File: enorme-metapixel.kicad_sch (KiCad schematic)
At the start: 22 parts, among them J1 VIN, J2 STRIP_0, J3 STRIP_1, J4 STRIP_2, J5 UART, J6 VIN, SW1 SW_RESET, SW2 SW_BOOT, U1 BD33FC0FP, U2 ESP32-WROOM-32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

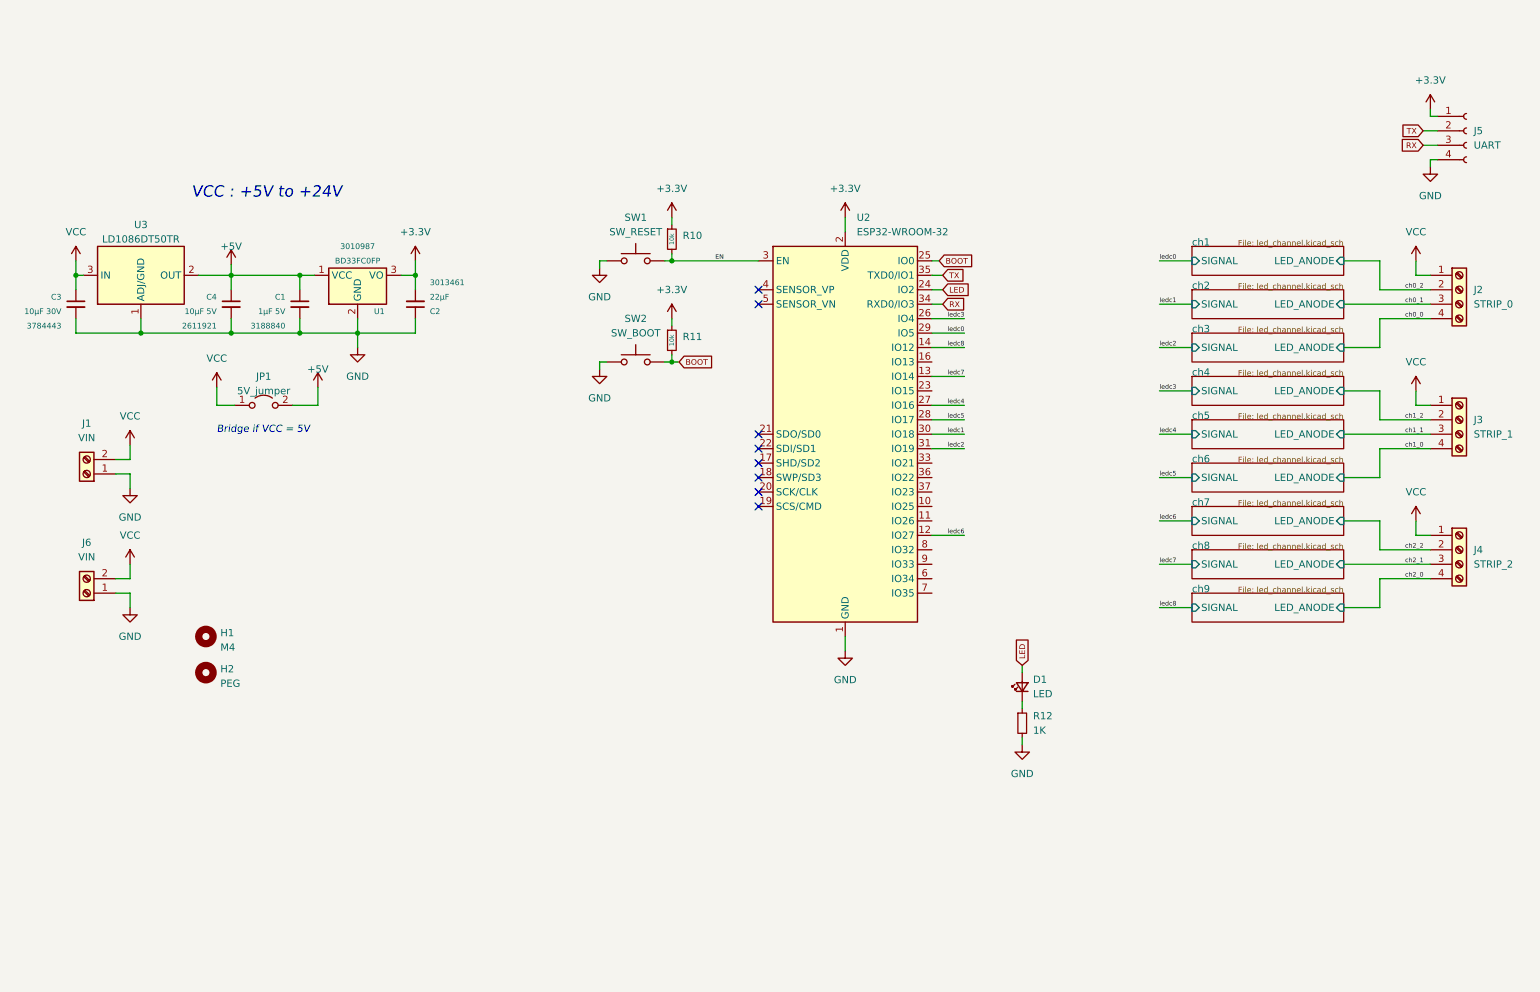
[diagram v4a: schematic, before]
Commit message: Rev 4 (replace LDO with buck converter)
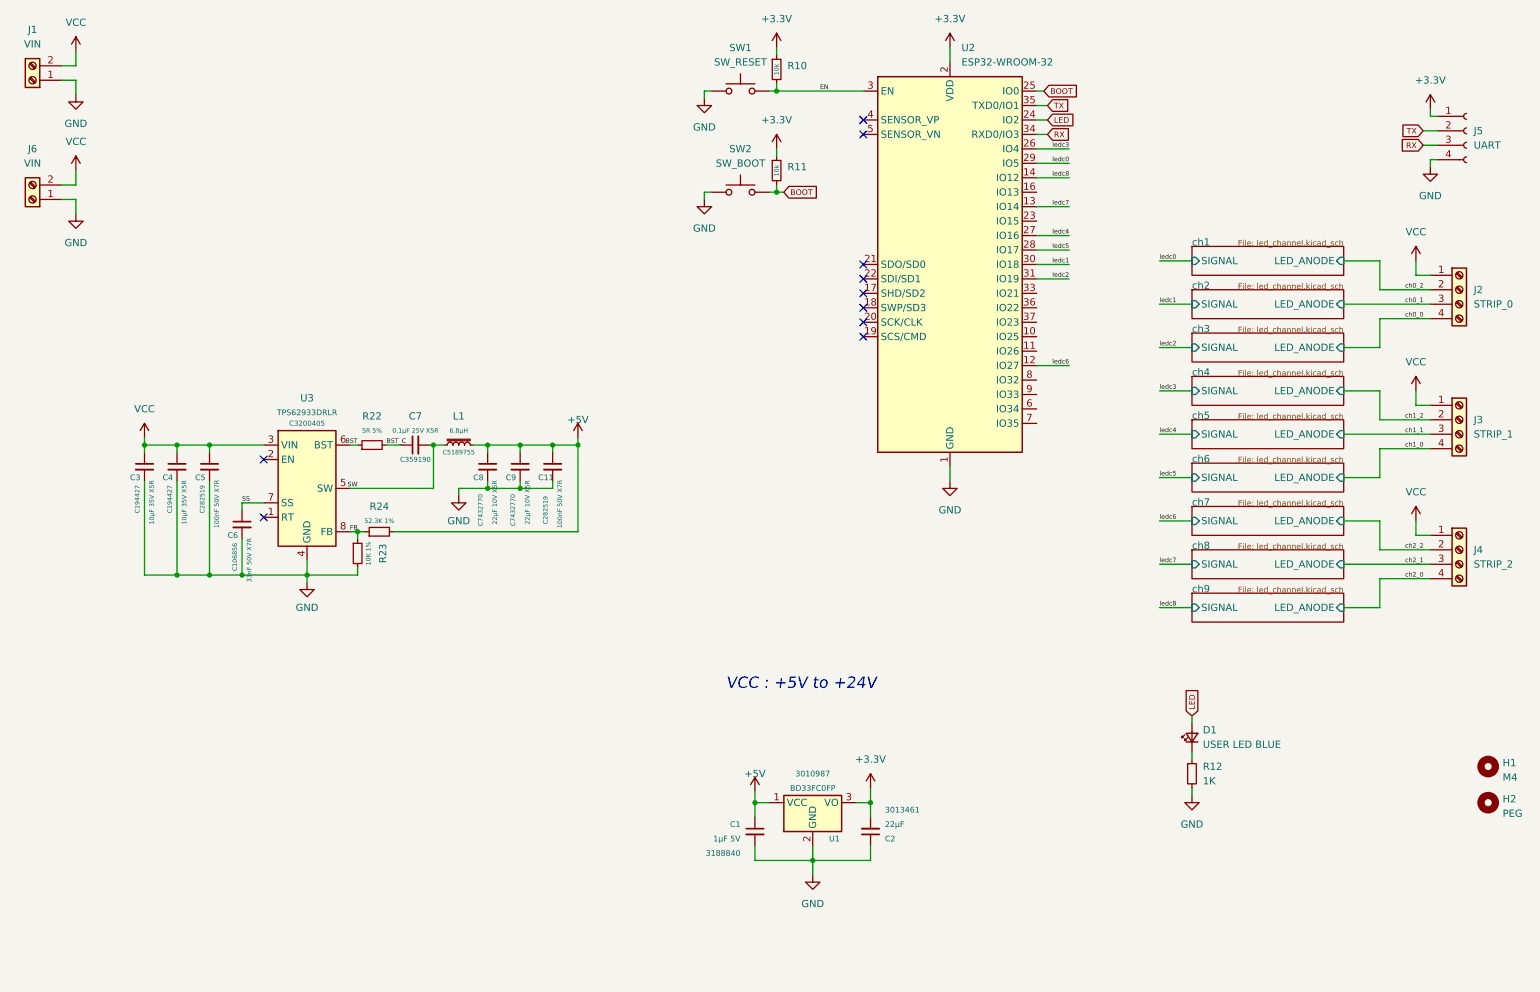
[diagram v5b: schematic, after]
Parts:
- removed JP1: 5V_jumper, Jumper:SolderJumper-2_P1.3mm_Open_RoundedPad1.0x1.5mm, symbol Jumper:Jumper_2_Open
- removed U3: LD1086DT50TR, Package_TO_SOT_SMD:TO-252-2, symbol Regulator_Linear:LD1086DT50TR
- added C11, C5: 100nF 50V X7R, Capacitor_SMD:C_0603_1608Metric, symbol Device:C_Small
- added C6: 33nF 50V X7R, Capacitor_SMD:C_0603_1608Metric, symbol Device:C_Small
- added C7: 0.1µF 25V X5R, Capacitor_SMD:C_0402_1005Metric, symbol Device:C_Small
- added C8, C9: 22µF 10V X5R, Capacitor_SMD:C_0603_1608Metric, symbol Device:C_Small
- added L1: 6.8µH, Inductor_SMD:L_Bourns_SRP7028A_7.3x6.6mm, symbol Device:L_Iron_Small
- added R22: 5R 5%, Resistor_SMD:R_0603_1608Metric, symbol Device:R_Small
- added R23: 10K 1%, Resistor_SMD:R_0603_1608Metric, symbol Device:R_Small
- added R24: 52.3K 1%, Resistor_SMD:R_0603_1608Metric, symbol Device:R_Small
- added U3: TPS62933DRLR, Package_TO_SOT_SMD:SOT-583-8, symbol Regulator_Switching:TPS62933
- C3: value 10µF 30V -> 10µF 35V X5R; Farnell 3784443 -> (none); LCSC (none) -> C194427
- C4: value 10µF 5V -> 10µF 35V X5R; Farnell 2611921 -> (none); LCSC (none) -> C194427
- D1: value LED -> USER LED BLUE
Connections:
- net +5V: now also C11.1, C8.1, C9.1, L1.2, R24.2; no longer C4.1
- net GND: now also C11.2, C5.2, C6.2, C8.2, C9.2, R23.2, U3.4 (GND)
- net VCC: now also C4.1, C5.1, U3.3 (VIN)
- new net BST: R22.1, U3.6 (BST)
- new net BST_C: C7.1, R22.2
- new net FB: R23.1, R24.1, U3.8 (FB)
- new net SS: C6.1, U3.7 (SS)
- new net SW: C7.2, L1.1, U3.5 (SW)
- no-connect marks 8 -> 10
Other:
- note removed: "Bridge if VCC = 5V"
- moved on the sheet: C1, C2, D1, H1, H2, J1, J6, R10, R11, R12, SW1, SW2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
